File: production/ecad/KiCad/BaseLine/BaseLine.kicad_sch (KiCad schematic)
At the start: 0 parts

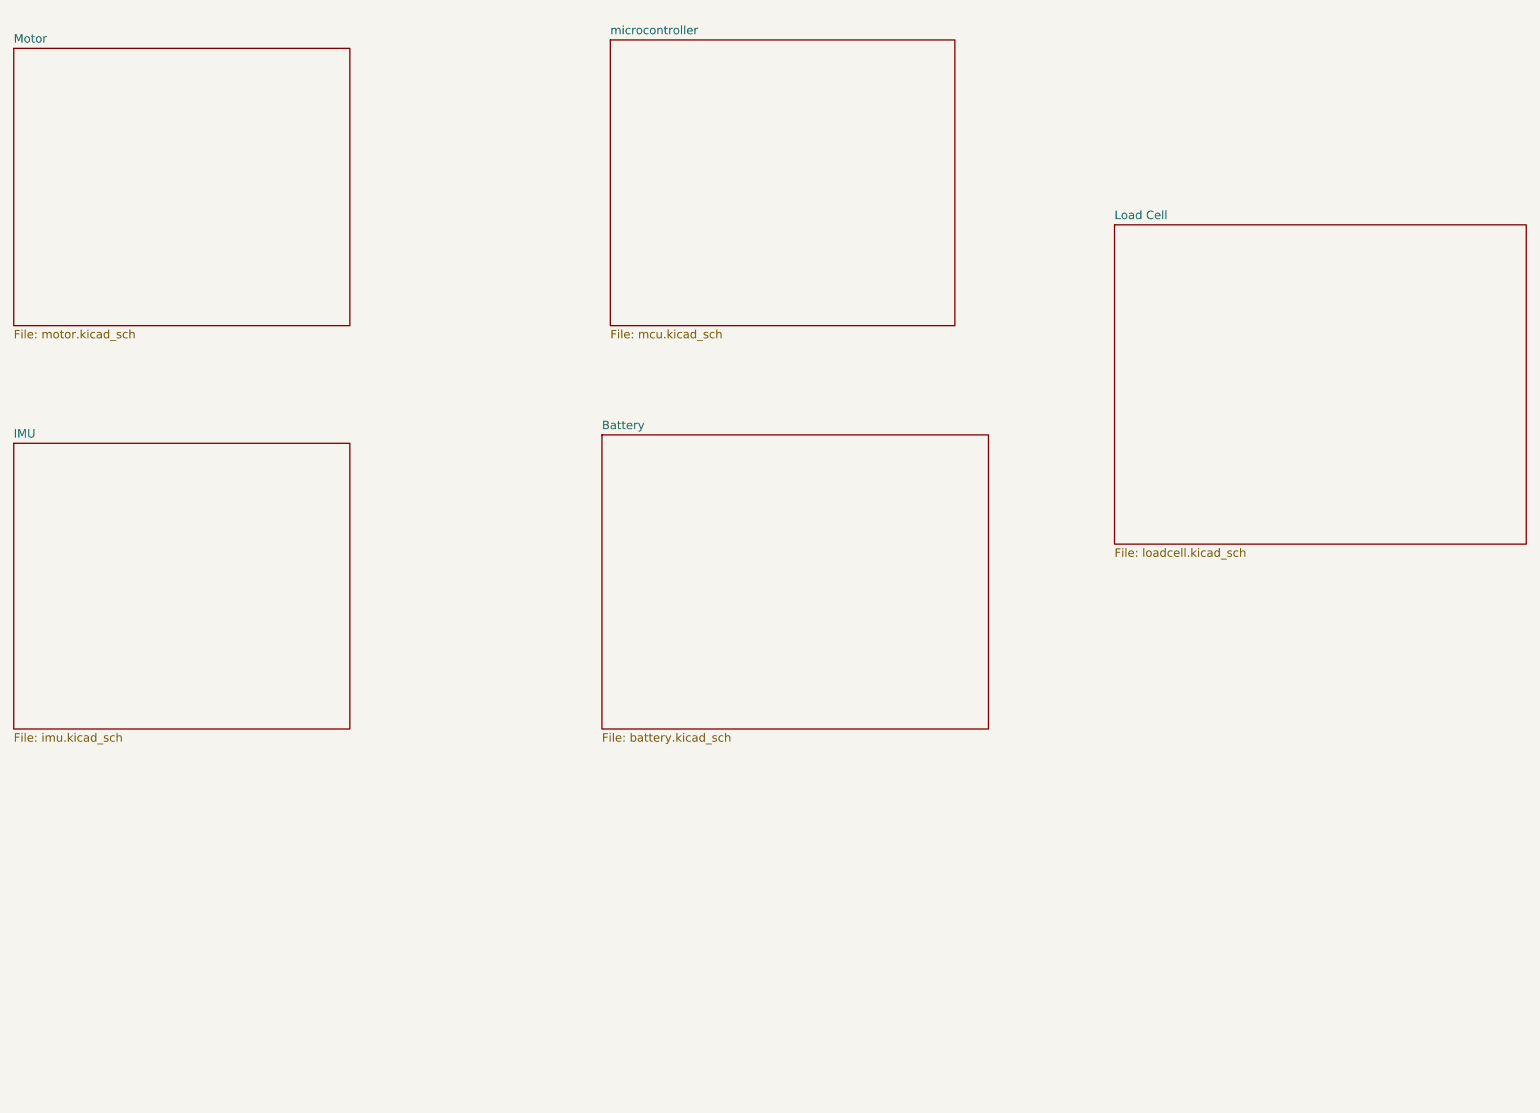
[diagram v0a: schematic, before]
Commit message: added rotary encoder schematic page
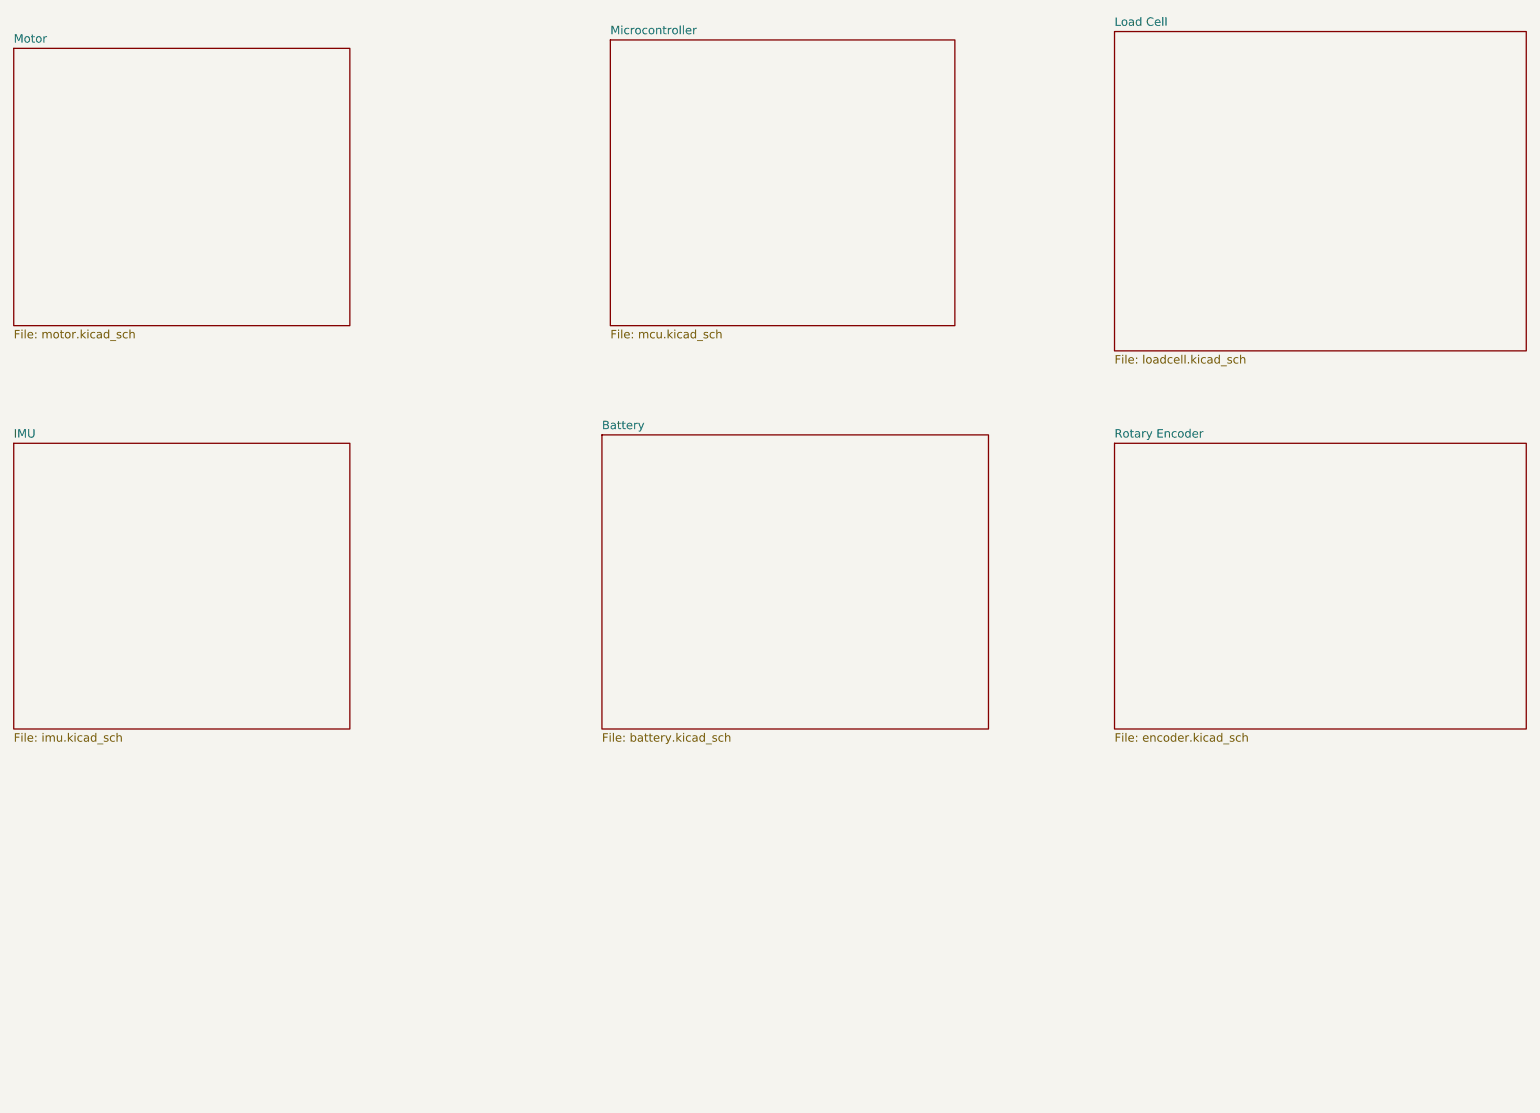
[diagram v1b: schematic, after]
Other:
- sheet microcontroller renamed Microcontroller
- added sheet Rotary Encoder (encoder.kicad_sch)
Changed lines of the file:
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@@
 	(paper "A4")
 	(sheet
-		(at 204.47 62.23)
+		(at 204.47 33.02)
 		(size 62.23 48.26)
 		(fields_autoplaced yes)
@@
 		)
 		(property "Sheetname" "Load Cell"
-			(at 204.47 61.5184 0)
+			(at 204.47 32.3084 0)
 			(effects
 				(font
@@
 		)
 		(property "Sheetfile" "loadcell.kicad_sch"
-			(at 204.47 111.0746 0)
+			(at 204.47 81.8646 0)
 			(effects
 				(font
@@
 	)
 	(sheet
+		(at 204.47 95.25)
+		(size 62.23 43.18)
+		(fields_autoplaced yes)
+		(stroke
+			(width 0.1524)
+			(type solid)
+		)
+		(fill
+			(color 0 0 0 0.0000)
+		)
+		(property "Sheetname" "Rotary Encoder"
+			(at 204.47 94.5384 0)
+			(effects
+				(font
+					(size 1.27 1.27)
+				)
+				(justify left bottom)
+			)
+		)
+		(property "Sheetfile" "encoder.kicad_sch"
+			(at 204.47 139.0146 0)
+			(effects
+				(font
+					(size 1.27 1.27)
+				)
+				(justify left top)
+			)
+		)
+		(instances
+			(project "BaseLine"
+				(path "/ba9eda21-3882-41e1-8265-3d8ac781da20"
+					(page "7")
+				)
+			)
+		)
+	)
+	(sheet
 		(at 128.27 34.29)
 		(size 52.07 43.18)
@@
 			(color 0 0 0 0.0000)
 		)
-		(property "Sheetname" "microcontroller"
+		(property "Sheetname" "Microcontroller"
 			(at 128.27 33.5784 0)
 			(effects

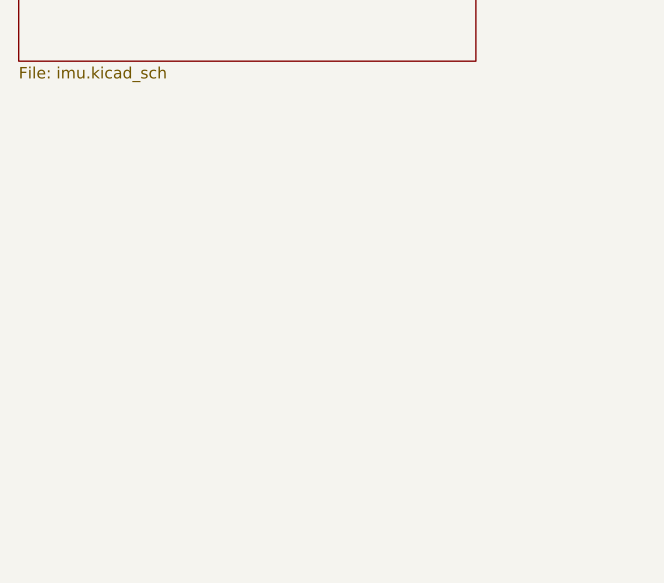
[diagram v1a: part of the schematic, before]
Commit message: MCU connections and matching names
matched the global net names of all the sensor connections with the MCU. Added an IO sheet for the power button
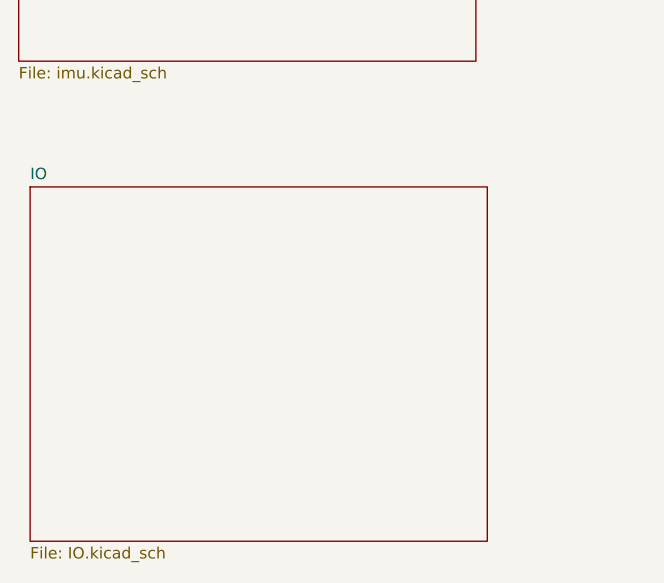
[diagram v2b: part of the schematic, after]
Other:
- added sheet IO (IO.kicad_sch)
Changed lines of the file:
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@@
+		)
+	)
+	(sheet
+		(at 39.37 152.4)
+		(size 50.8 39.37)
+		(fields_autoplaced yes)
+		(stroke
+			(width 0.1524)
+			(type solid)
+		)
+		(fill
+			(color 0 0 0 0.0000)
+		)
+		(property "Sheetname" "IO"
+			(at 39.37 151.6884 0)
+			(effects
+				(font
+					(size 1.27 1.27)
+				)
+				(justify left bottom)
+			)
+		)
+		(property "Sheetfile" "IO.kicad_sch"
+			(at 39.37 192.3546 0)
+			(effects
+				(font
+					(size 1.27 1.27)
+				)
+				(justify left top)
+			)
+		)
+		(instances
+			(project "BaseLine"
+				(path "/ba9eda21-3882-41e1-8265-3d8ac781da20"
+					(page "8")
+				)
+			)
 		)
 	)

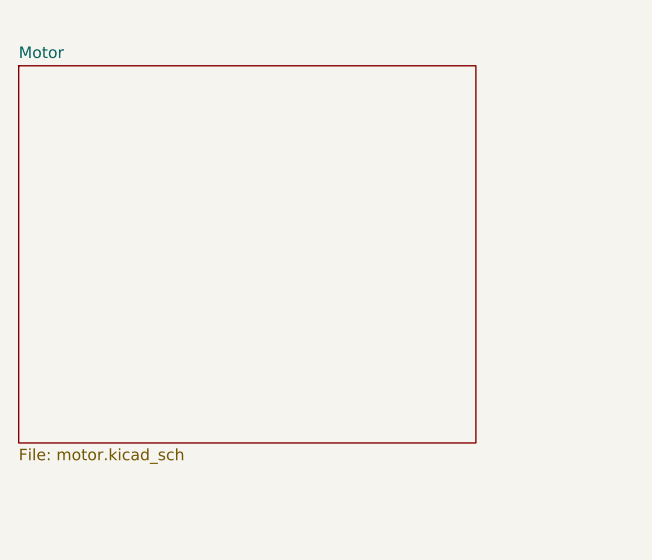
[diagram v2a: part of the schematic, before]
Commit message: Load cell updates
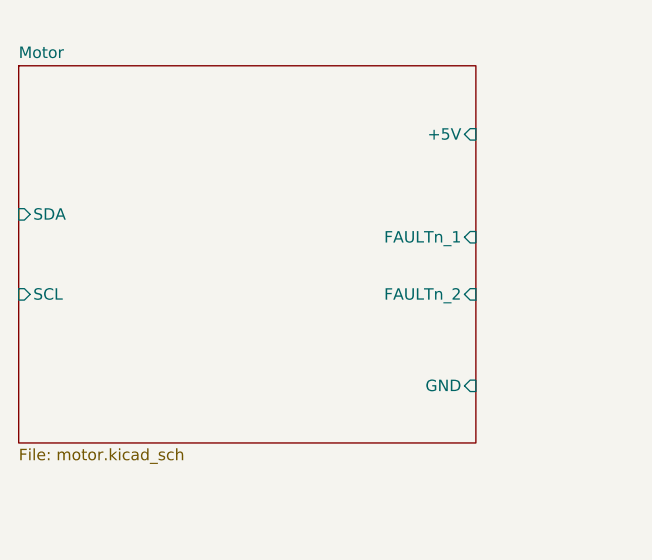
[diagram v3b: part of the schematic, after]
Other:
- sheet Motor ports: added +5V, FAULTn_1, FAULTn_2, GND, SCL, SDA; removed none
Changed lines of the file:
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@@
+			)
+		)
+		(pin "GND" input
+			(at 88.9 71.12 0)
+			(effects
+				(font
+					(size 1.27 1.27)
+				)
+				(justify right)
+			)
+		)
+		(pin "+5V" input
+			(at 88.9 43.18 0)
+			(effects
+				(font
+					(size 1.27 1.27)
+				)
+				(justify right)
+			)
+		)
+		(pin "SDA" input
+			(at 38.1 52.07 180)
+			(effects
+				(font
+					(size 1.27 1.27)
+				)
+				(justify left)
+			)
+		)
+		(pin "SCL" input
+			(at 38.1 60.96 180)
+			(effects
+				(font
+					(size 1.27 1.27)
+				)
+				(justify left)
+			)
+		)
+		(pin "FAULTn_1" input
+			(at 88.9 54.61 0)
+			(effects
+				(font
+					(size 1.27 1.27)
+				)
+				(justify right)
+			)
+		)
+		(pin "FAULTn_2" input
+			(at 88.9 60.96 0)
+			(effects
+				(font
+					(size 1.27 1.27)
+				)
+				(justify right)
 			)
 		)

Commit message: adding heirarchal pins
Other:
- sheet Battery ports: added +3.3V, +5V; removed none
- sheet Rotary Encoder ports: added +3.3V, +5V, +GND, CLK_rotaryenc, CS_rotaryenc, DO_rotaryenc; removed none
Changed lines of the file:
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@@
+			)
+		)
+		(pin "+3.3V" input
+			(at 143.51 93.98 90)
+			(effects
+				(font
+					(size 1.27 1.27)
+				)
+				(justify right)
+			)
+		)
+		(pin "+5V" input
+			(at 154.94 93.98 90)
+			(effects
+				(font
+					(size 1.27 1.27)
+				)
+				(justify right)
 			)
 		)
@@
 			)
 		)
+		(pin "CLK_rotaryenc" input
+			(at 204.47 104.14 180)
+			(effects
+				(font
+					(size 1.27 1.27)
+				)
+				(justify left)
+			)
+		)
+		(pin "DO_rotaryenc" output
+			(at 204.47 110.49 180)
+			(effects
+				(font
+					(size 1.27 1.27)
+				)
+				(justify left)
+			)
+		)
+		(pin "CS_rotaryenc" input
+			(at 204.47 116.84 180)
+			(effects
+				(font
+					(size 1.27 1.27)
+				)
+				(justify left)
+			)
+		)
+		(pin "+3.3V" input
+			(at 204.47 123.19 180)
+			(effects
+				(font
+					(size 1.27 1.27)
+				)
+				(justify left)
+			)
+		)
+		(pin "+5V" input
+			(at 204.47 129.54 180)
+			(effects
+				(font
+					(size 1.27 1.27)
+				)
+				(justify left)
+			)
+		)
+		(pin "+GND" input
+			(at 204.47 134.62 180)
+			(effects
+				(font
+					(size 1.27 1.27)
+				)
+				(justify left)
+			)
+		)

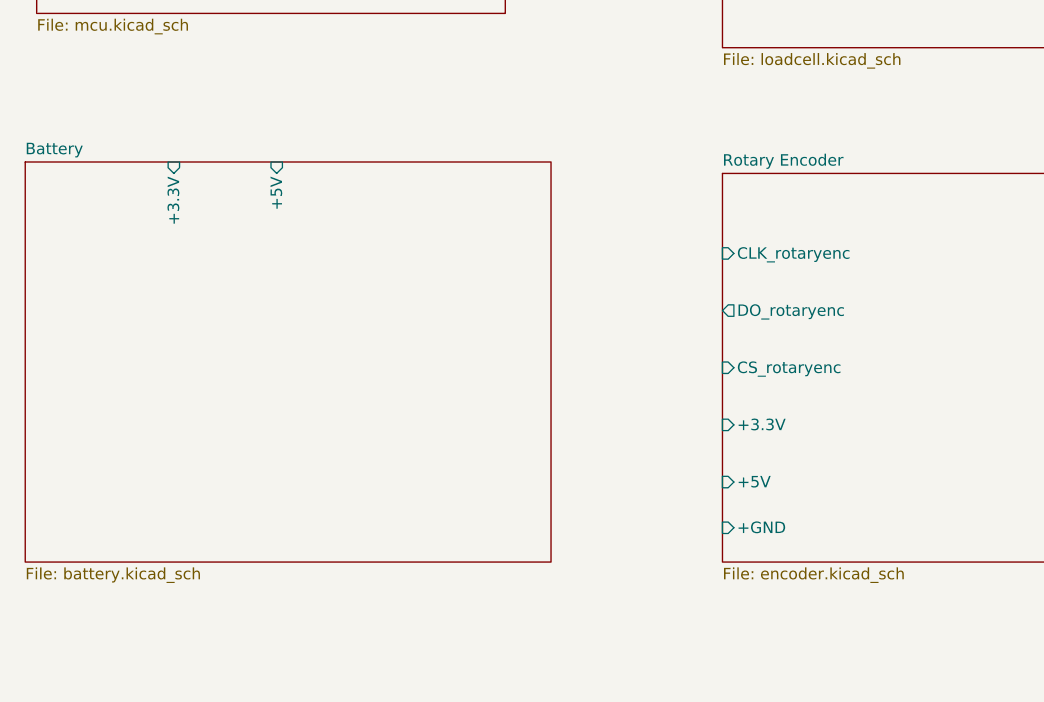
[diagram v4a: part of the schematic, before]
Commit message: Updated more footprints
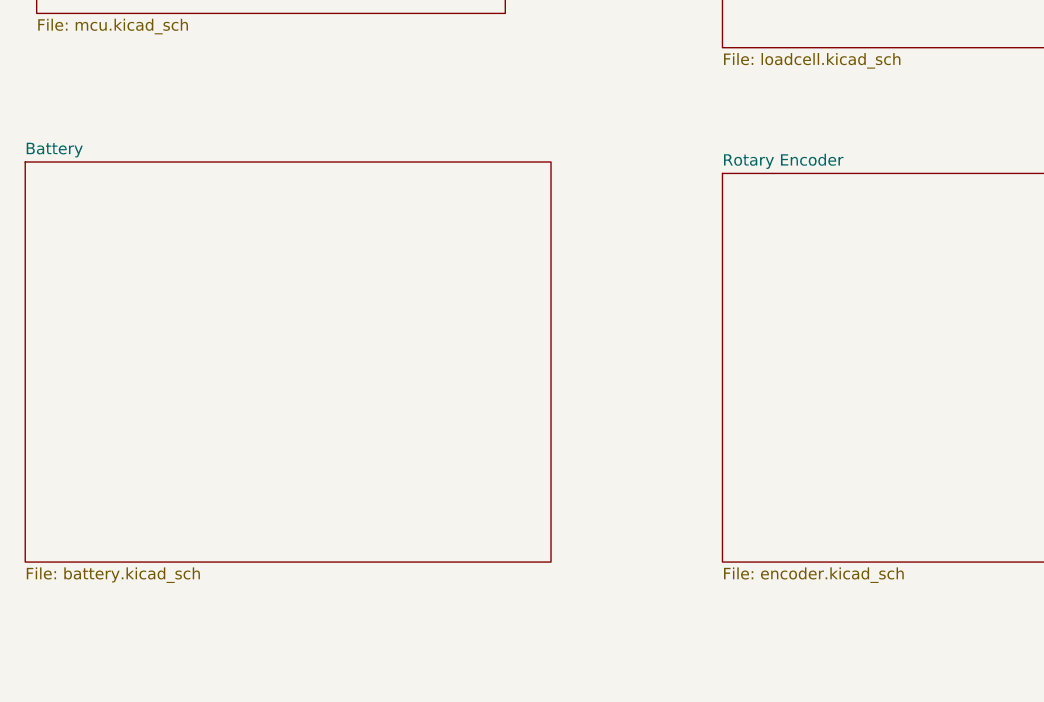
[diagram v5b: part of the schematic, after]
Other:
- sheet Battery ports: added none; removed +3.3V, +5V
- sheet Rotary Encoder ports: added none; removed +3.3V, +5V, +GND, CLK_rotaryenc, CS_rotaryenc, DO_rotaryenc
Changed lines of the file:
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@@
-			)
-		)
-		(pin "+3.3V" input
-			(at 143.51 93.98 90)
-			(effects
-				(font
-					(size 1.27 1.27)
-				)
-				(justify right)
-			)
-		)
-		(pin "+5V" input
-			(at 154.94 93.98 90)
-			(effects
-				(font
-					(size 1.27 1.27)
-				)
-				(justify right)
 			)
 		)
@@
 			)
 		)
-		(pin "CLK_rotaryenc" input
-			(at 204.47 104.14 180)
-			(effects
-				(font
-					(size 1.27 1.27)
-				)
-				(justify left)
-			)
-		)
-		(pin "DO_rotaryenc" output
-			(at 204.47 110.49 180)
-			(effects
-				(font
-					(size 1.27 1.27)
-				)
-				(justify left)
-			)
-		)
-		(pin "CS_rotaryenc" input
-			(at 204.47 116.84 180)
-			(effects
-				(font
-					(size 1.27 1.27)
-				)
-				(justify left)
-			)
-		)
-		(pin "+3.3V" input
-			(at 204.47 123.19 180)
-			(effects
-				(font
-					(size 1.27 1.27)
-				)
-				(justify left)
-			)
-		)
-		(pin "+5V" input
-			(at 204.47 129.54 180)
-			(effects
-				(font
-					(size 1.27 1.27)
-				)
-				(justify left)
-			)
-		)
-		(pin "+GND" input
-			(at 204.47 134.62 180)
-			(effects
-				(font
-					(size 1.27 1.27)
-				)
-				(justify left)
-			)
-		)

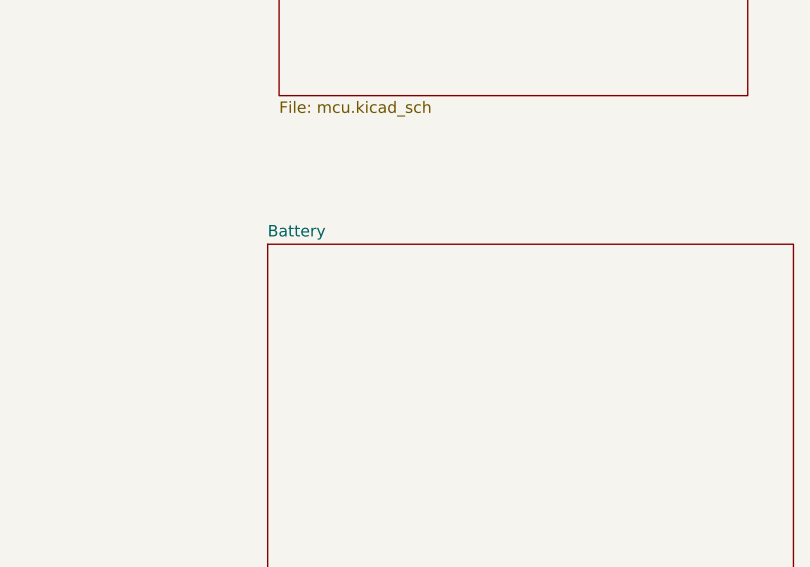
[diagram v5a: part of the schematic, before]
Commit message: added some heirarchal pins
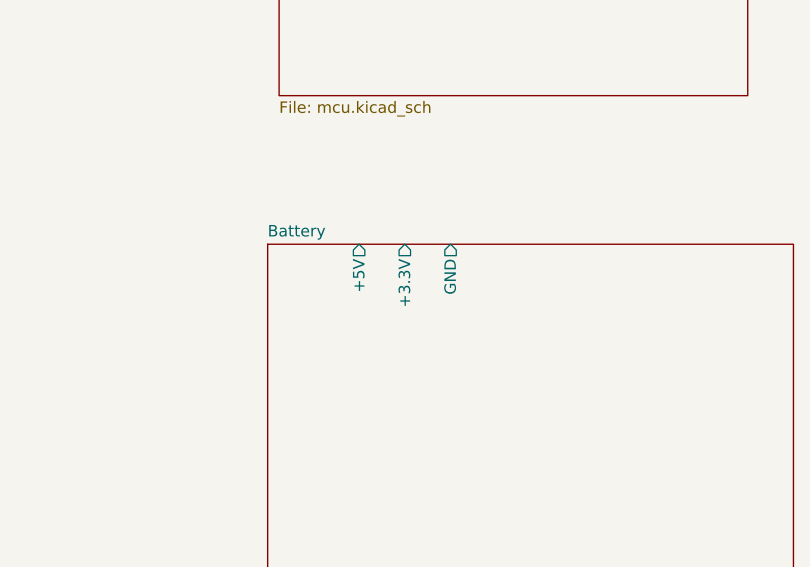
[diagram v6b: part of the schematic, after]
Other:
- sheet Battery ports: added +3.3V, +5V, GND; removed none
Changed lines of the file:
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@@
+			)
+		)
+		(pin "+3.3V" output
+			(at 142.24 93.98 90)
+			(effects
+				(font
+					(size 1.27 1.27)
+				)
+				(justify right)
+			)
+		)
+		(pin "GND" output
+			(at 147.32 93.98 90)
+			(effects
+				(font
+					(size 1.27 1.27)
+				)
+				(justify right)
+			)
+		)
+		(pin "+5V" output
+			(at 137.16 93.98 90)
+			(effects
+				(font
+					(size 1.27 1.27)
+				)
+				(justify right)
 			)
 		)
